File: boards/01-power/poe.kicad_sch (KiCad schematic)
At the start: 1 part, among them U4 PMIC_TPS2372_4RGWR

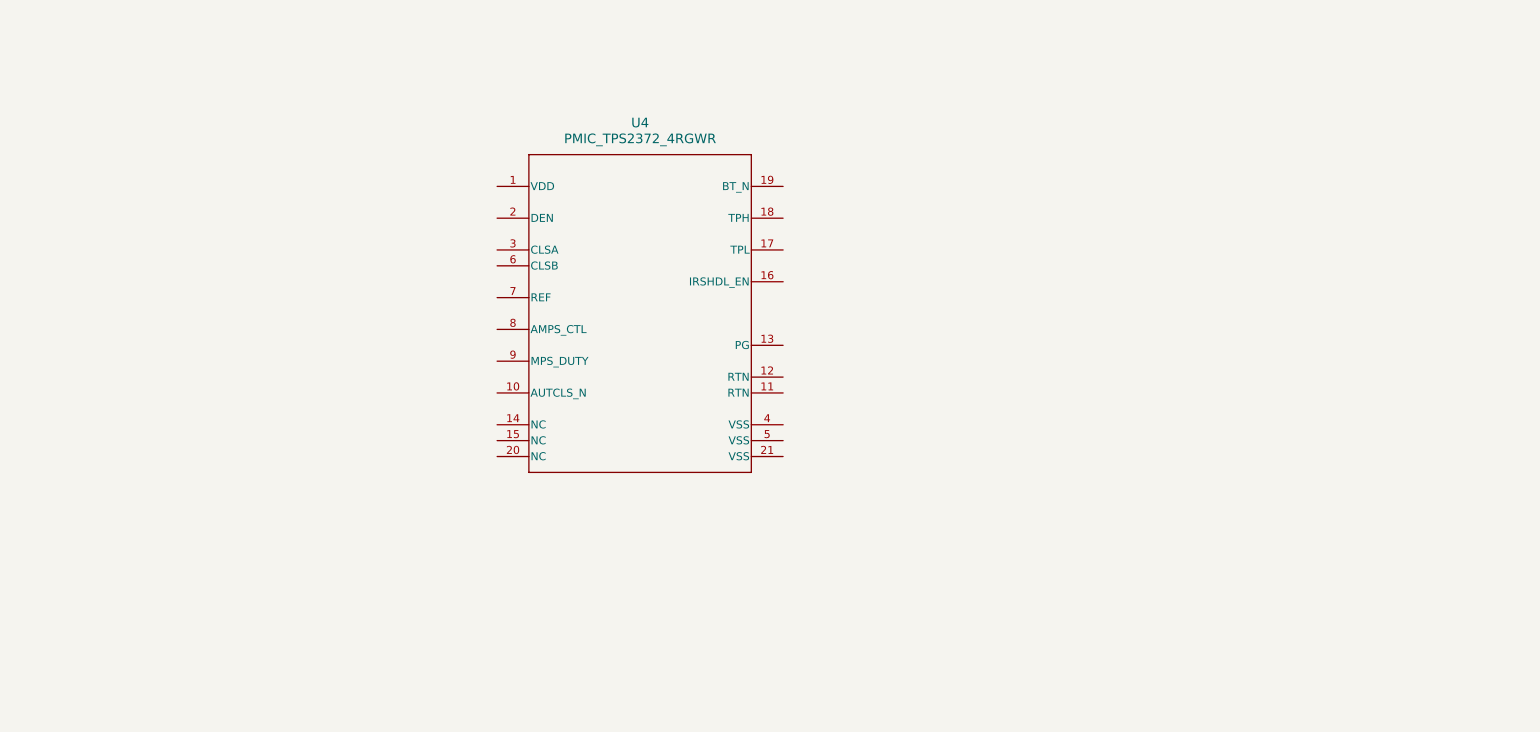
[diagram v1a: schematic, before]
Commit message: poe: class 8 negotiate(max around 62W-71W at PD)
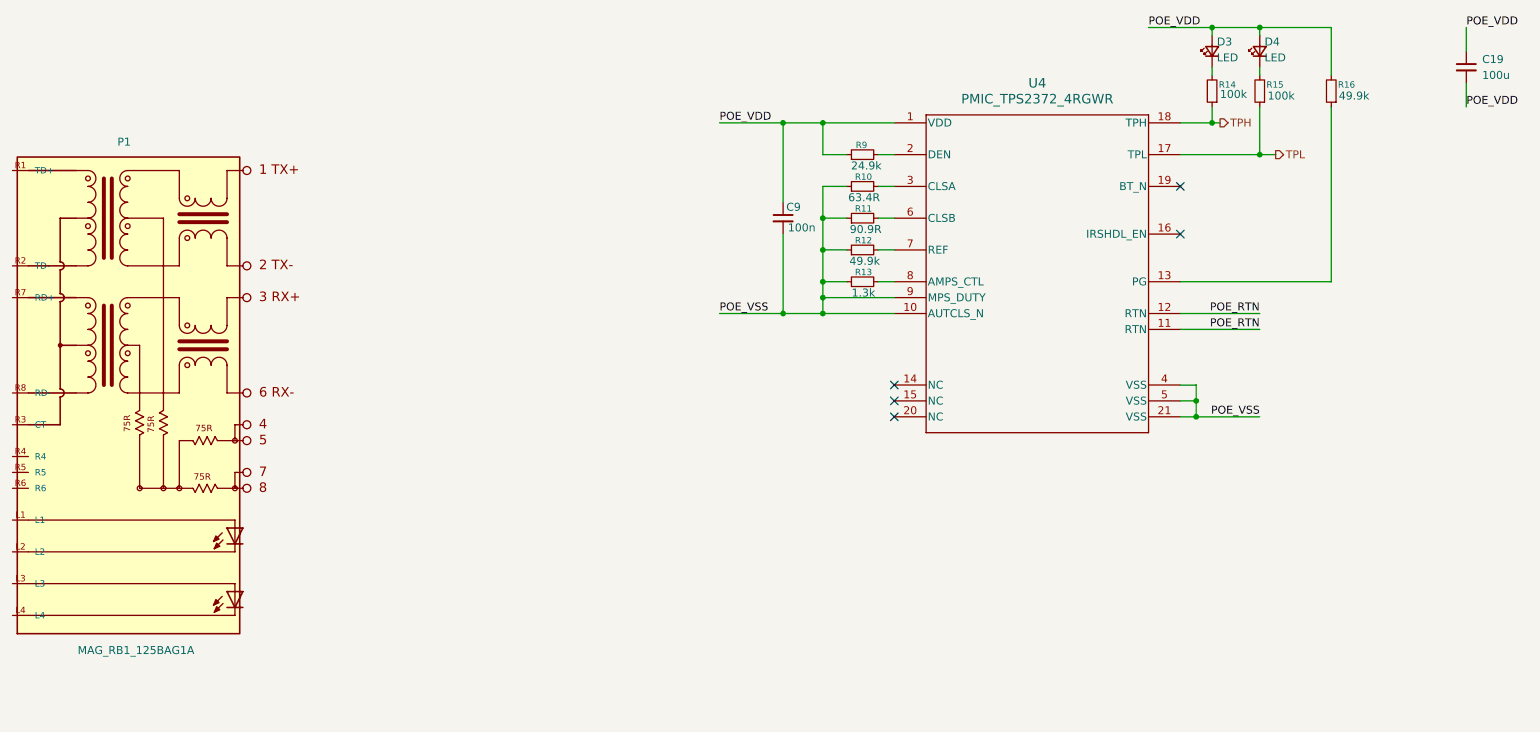
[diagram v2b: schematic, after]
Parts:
- added C19: 100u, symbol Device:C_Small
- added C9: 100n, symbol Device:C_Small
- added D3, D4: LED, symbol Device:LED_Small
- added P1: MAG_RB1_125BAG1A, Woki:MAG_RB1_125BAG1A, symbol ETH:MAG_RB1_125BAG1A
- added R10: 63.4R, symbol Device:R_Small
- added R11: 90.9R, symbol Device:R_Small
- added R12, R16: 49.9k, symbol Device:R_Small
- added R13: 1.3k, symbol Device:R_Small
- added R14, R15: 100k, symbol Device:R_Small
- added R9: 24.9k, symbol Device:R_Small
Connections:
- net POE_VDD: now reaches U4.1 (VDD)
- net POE_VDD: now also C19.1, C19.2, C9.1, D3.2 (A), D4.2 (A), R16.2, R9.1
- net POE_VSS: now reaches U4.10 (AUTCLS_N)
- net POE_VSS: now also U4.21 (VSS), U4.4 (VSS), U4.5 (VSS), U4.9 (MPS_DUTY), C9.2, R10.1, R11.1, R12.1, R13.1
- net POE_RTN: now reaches U4.11 (RTN)
- net POE_RTN: now also U4.12 (RTN)
- net at U4.13 (PG): now also R16.1
- net TPL: now reaches U4.17 (TPL)
- net TPL: now also R15.1
- net TPH: now reaches U4.18 (TPH)
- net TPH: now also R14.1
- net at U4.2 (DEN): now also R9.2
- net at U4.3 (CLSA): now also R10.2
- net at U4.6 (CLSB): now also R11.2
- net at U4.7 (REF): now also R12.2
- net at U4.8 (AMPS_CTL): now also R13.2
- new net: D3.1 (K), R14.2
- new net: D4.1 (K), R15.2
- no-connect marks 0 -> 5

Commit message: poe: magjack
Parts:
- added D10, D11, D12, D5, D6, D7, D8, D9: D, symbol Device:D_Schottky_Small
- C19: footprint (none) -> Capacitor_SMD:CP_Elec_8x10
- C9: footprint (none) -> Capacitor_SMD:C_0603_1608Metric
- D3, D4: footprint (none) -> LED_SMD:LED_0603_1608Metric
- P1: Availability In Stock -> (none); Check_prices https://www.snapeda.com/parts/RB1-125BAG1A/WIZnet/view-part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 -> (none); MANUFACTURER WIZnet -> (none); MF WIZnet -> (none); MP RB1-125BAG1A -> (none); Package None -> (none); Price None -> (none); SnapEDA_Link https://www.snapeda.com/parts/RB1-125BAG1A/WIZnet/view-part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 -> (none)
- R10, R11, R12, R14, R15, R16, R9: footprint (none) -> Resistor_SMD:R_0603_1608Metric
- R13: footprint (none) -> Resistor_SMD:R_0805_2012Metric
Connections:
- net POE_VDD: no longer C19.2
- net POE_VSS: now also C19.2
- new net: D11.1 (K), D12.1 (K)
- new net: D11.2 (A), D9.1 (K)
- new net: D10.1 (K), D12.2 (A)
- new net: D10.2 (A), D9.2 (A)
- new net: D5.1 (K), D6.2 (A)
- new net: D5.2 (A), D7.2 (A)
- new net: D6.1 (K), D8.1 (K)
- new net: D7.1 (K), D8.2 (A)
